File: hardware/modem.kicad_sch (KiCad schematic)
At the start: 33 parts, among them J13 PRPC001DAAN-RC, Q5 IRLML2246TRPBF, Q6 MMBT3904, U10 SARA-R500S-61B, U8 74AVC1T45DW-7, U9 74AVC1T45DW-7

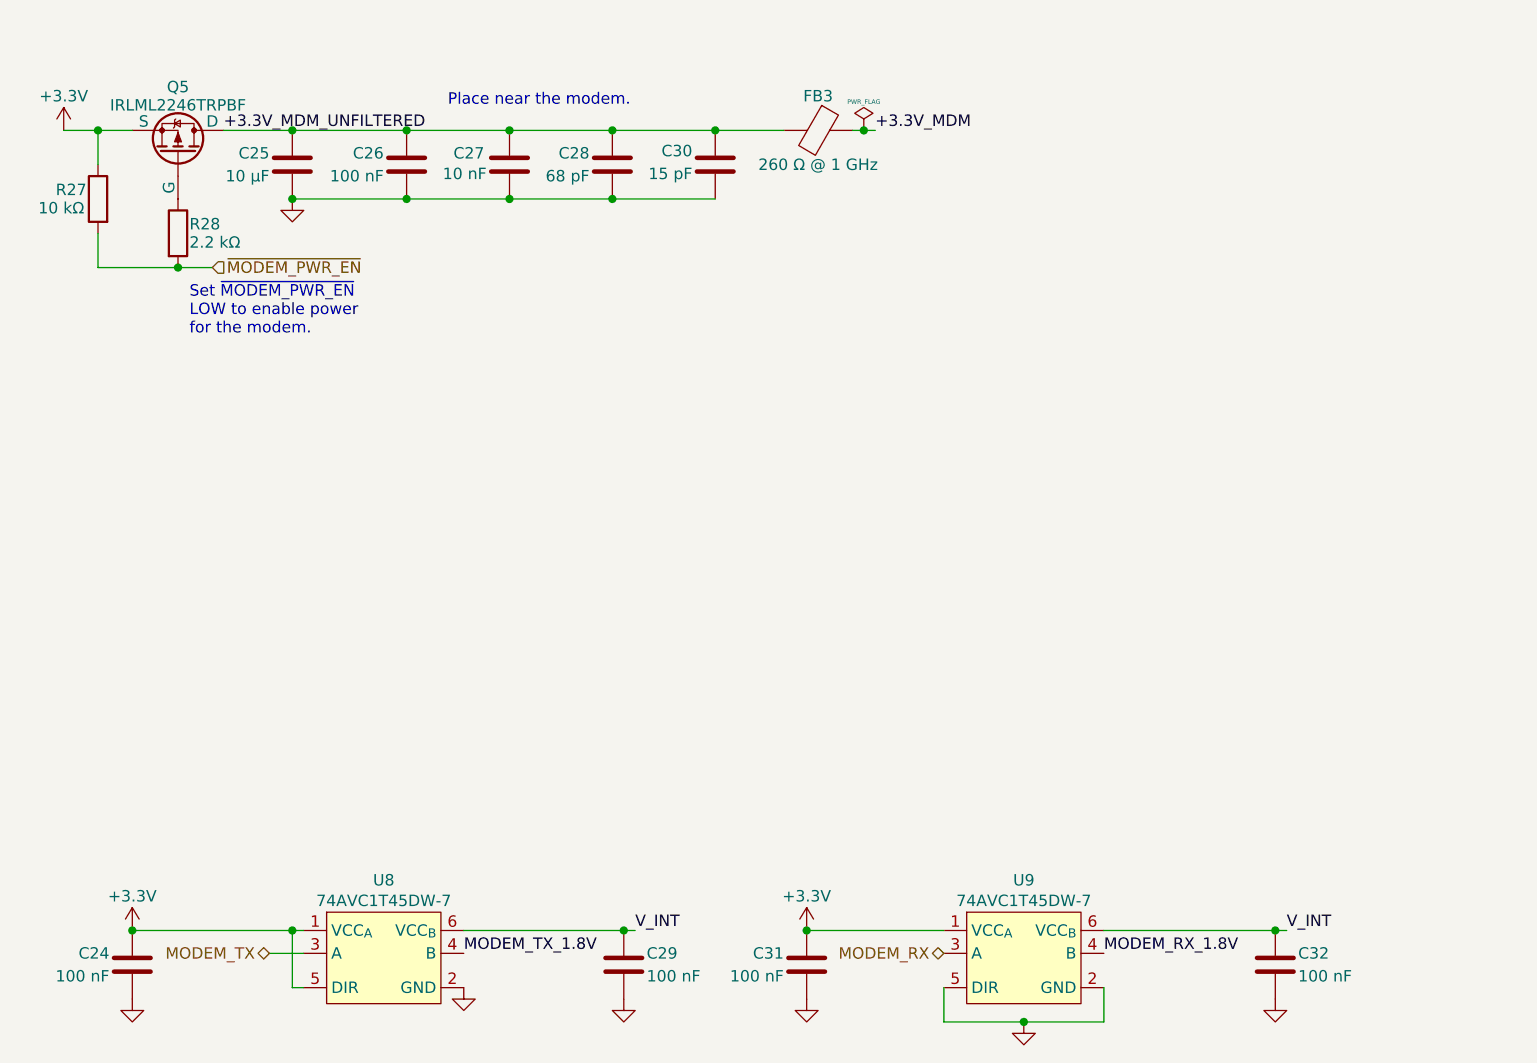
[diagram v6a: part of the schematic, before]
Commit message: HW: Replace 0402 with 0603 or bigger
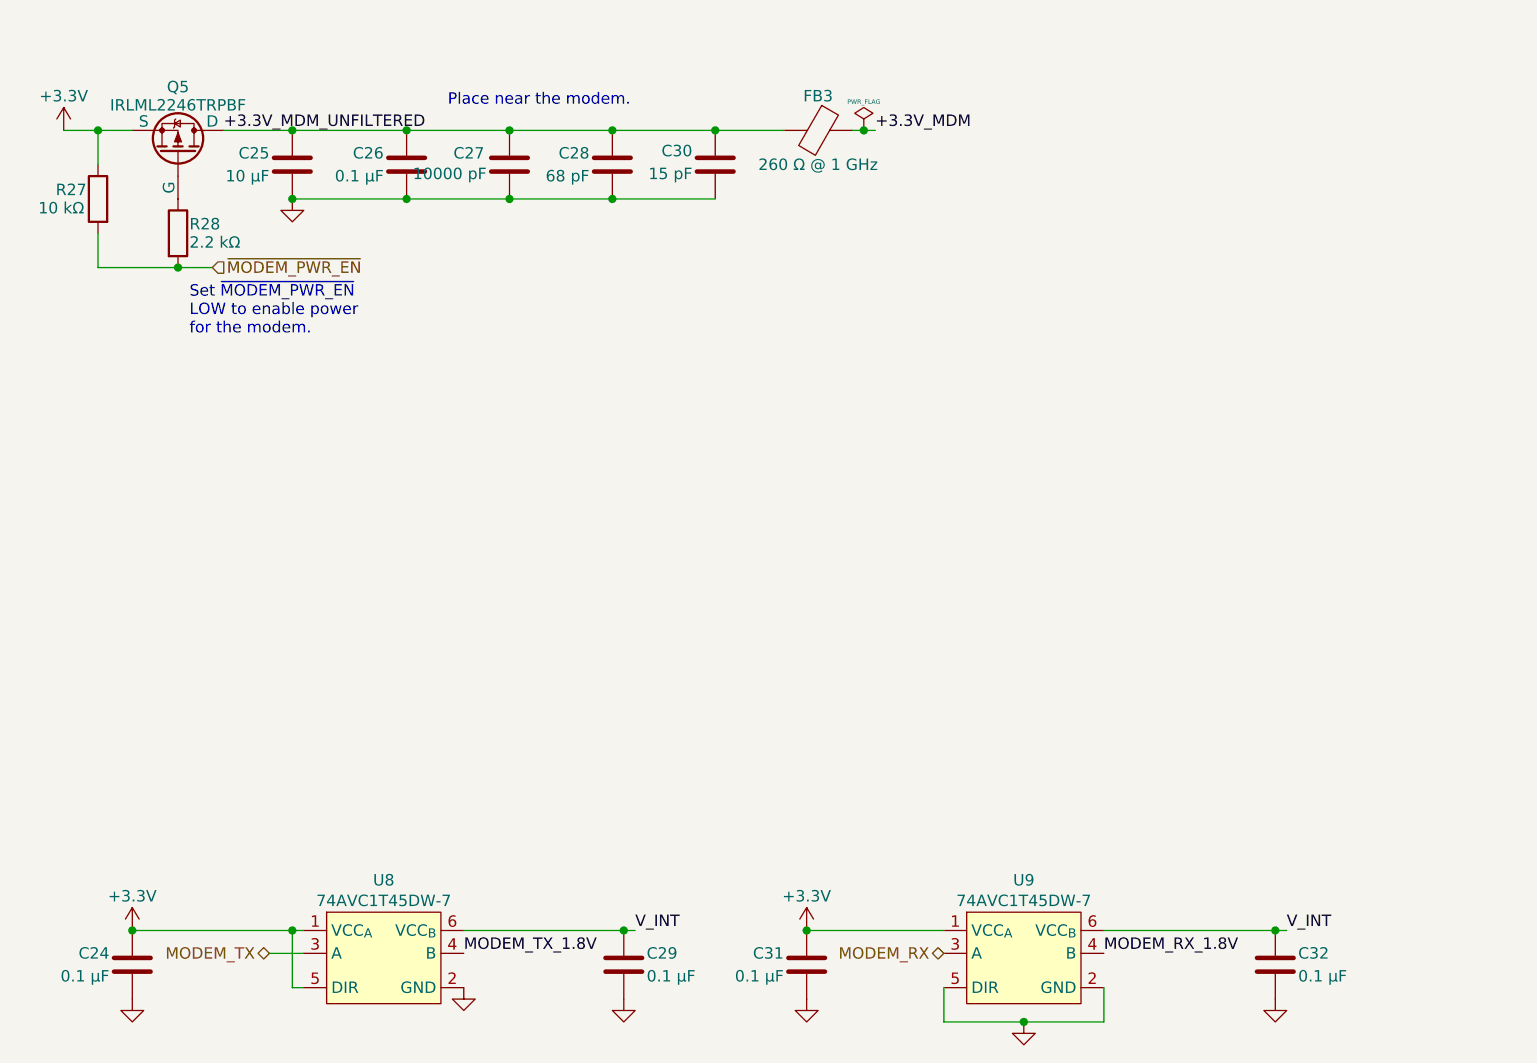
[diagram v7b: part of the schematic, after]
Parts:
- C24, C26, C29, C31, C32: value 100 nF -> 0.1 µF; footprint Capacitor_SMD:C_0402_1005Metric_Pad0.74x0.62mm_HandSolder -> Capacitor_SMD:C_0603_1608Metric_Pad1.08x0.95mm_HandSolder; Digi-Key Part Number 732-7513-1-ND -> 732-7989-1-ND; Manufacturer Part Number 885012205018 -> 885012206071
- C25: Digi-Key Part Number 490-3896-1-ND -> 732-7903-1-ND; Manufacturer Murata Electronics -> Würth Elektronik; Manufacturer Part Number GRM188R60J106ME47D -> 885012106006
- C27: value 10 nF -> 10000 pF; footprint Capacitor_SMD:C_0402_1005Metric_Pad0.74x0.62mm_HandSolder -> Capacitor_SMD:C_0603_1608Metric_Pad1.08x0.95mm_HandSolder; Digi-Key Part Number 490-GRT155R71C103KE01JCT-ND -> 732-8007-1-ND; Manufacturer Murata Electronics -> Würth Elektronik; Manufacturer Part Number GRT155R71C103KE01J -> 885012206089
- C28: footprint Capacitor_SMD:C_0402_1005Metric_Pad0.74x0.62mm_HandSolder -> Capacitor_SMD:C_0603_1608Metric_Pad1.08x0.95mm_HandSolder; Digi-Key Part Number 732-7474-1-ND -> 732-7779-1-ND; Manufacturer Part Number 885012005060 -> 885012006037
- C30: footprint Capacitor_SMD:C_0402_1005Metric_Pad0.74x0.62mm_HandSolder -> Capacitor_SMD:C_0603_1608Metric_Pad1.08x0.95mm_HandSolder; Digi-Key Part Number 732-7470-1-ND -> 732-7747-1-ND; Manufacturer Part Number 885012005056 -> 885012006003
- R27, R31, R32, R33, R34: footprint Resistor_SMD:R_0402_1005Metric_Pad0.72x0.64mm_HandSolder -> Resistor_SMD:R_0603_1608Metric_Pad0.98x0.95mm_HandSolder; Digi-Key Part Number 732-560112110020CT-ND -> 732-560112116005CT-ND; Manufacturer Part Number 560112110020 -> 560112116005
- R28, R29: footprint Resistor_SMD:R_0402_1005Metric_Pad0.72x0.64mm_HandSolder -> Resistor_SMD:R_0603_1608Metric_Pad0.98x0.95mm_HandSolder; Digi-Key Part Number 732-560112110087CT-ND -> 732-560112116098CT-ND; Manufacturer Part Number 560112110087 -> 560112116098
- R30, R35, R36: footprint Resistor_SMD:R_0402_1005Metric_Pad0.72x0.64mm_HandSolder -> Resistor_SMD:R_0805_2012Metric_Pad1.20x1.40mm_HandSolder; Digi-Key Part Number 732-560112110001CT-ND -> 732-560112120002CT-ND; Manufacturer Part Number 560112110001 -> 560112120002

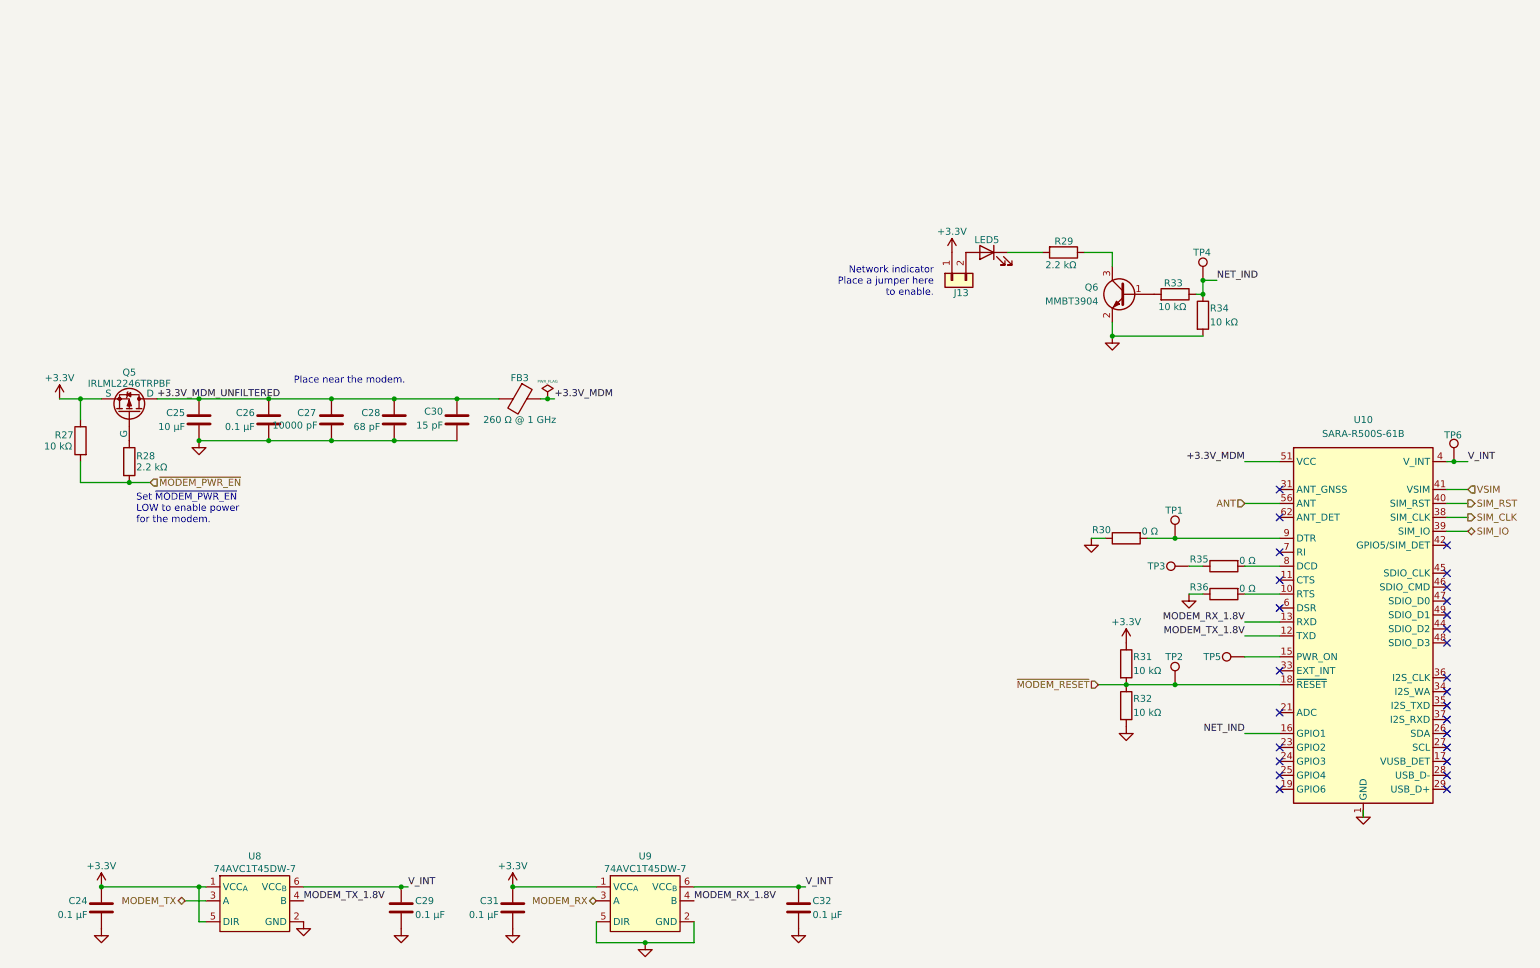
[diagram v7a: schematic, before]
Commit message: HW: Cleanup schematic
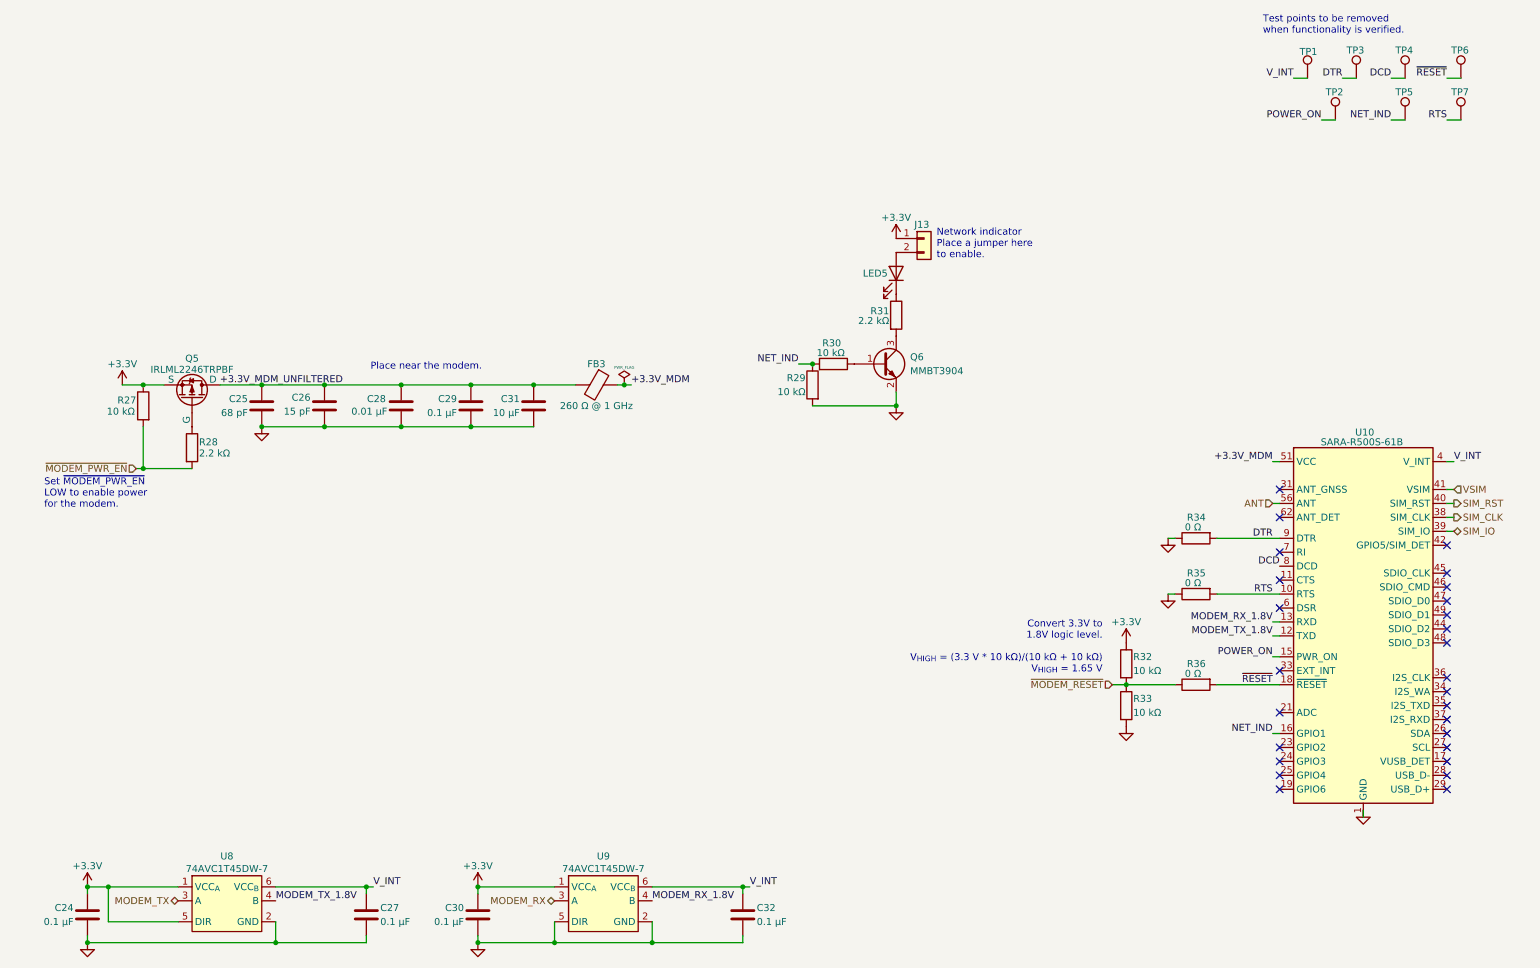
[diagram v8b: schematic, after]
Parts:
- removed R35: 0 Ω, Resistor_SMD:R_0805_2012Metric_Pad1.20x1.40mm_HandSolder, symbol Device:R
- removed TP6: TestPoint, TestPoint:TestPoint_Pad_D1.5mm, symbol Connector:TestPoint
- added R36: 0 Ω, Resistor_SMD:R_0805_2012Metric_Pad1.20x1.40mm_HandSolder, symbol Device:R
- added TP3, TP7: TestPoint, TestPoint:TestPoint_Pad_D1.5mm, symbol Connector:TestPoint
- C28: renamed from C27; value 10000 pF -> 0.01 µF
- renumbered C28 to C25, C30 to C26, C29 to C27, C26 to C29, C31 to C30, C25 to C31, R34 to R29, R33 to R30, R29 to R31, R31 to R32, R32 to R33, R30 to R34, R36 to R35, TP5 to TP2, TP3 to TP4, TP4 to TP5, TP2 to TP6
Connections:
- net NET_IND: now also R30.2; no longer R30.1
- net V_INT: now also TP1.1
- net ~{MODEM_RESET}: now also R36.1; no longer TP6.1, U10.18 (~{RESET})
- net at LED5.1 (K): now also R31.1; no longer R31.2
- net DCD: now reaches TP4.1
- net DCD: now also U10.8 (DCD)
- net at Q6.1 (B): now also R30.1; no longer R30.2
- net DTR: now reaches R34.2, U10.9 (DTR)
- net DTR: now also TP3.1; no longer TP1.1
- net RTS: now reaches R35.2, U10.10 (RTS)
- net RTS: now also TP7.1
- net at Q6.3 (C): now also R31.2; no longer R31.1
- net POWER_ON: now reaches TP2.1, U10.15 (PWR_ON)
- new net ~{RESET}: R36.2, TP6.1, U10.18 (~{RESET})
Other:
- note added: "Convert 3.3V to 1.8V logic level. V_{HIGH} = (3.3 V * 10 kΩ)/(10 kΩ + 10 kΩ) V_{HIGH} = 1.65 V"
- note added: "Test points to be removed when functionality is verified."
- moved on the sheet: C24, C25, C26, C27, C28, C29, C30, C31, C32, FB3, J13, LED5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
